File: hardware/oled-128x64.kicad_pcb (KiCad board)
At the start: 2 copper layers, 45 x 25 mm, 24 parts, among them P1 CON-SENSOR, U1 M24C64, U2 OLED013, U3 DRILL, U4 DRILL, U5 DRILL, U6 DRILL

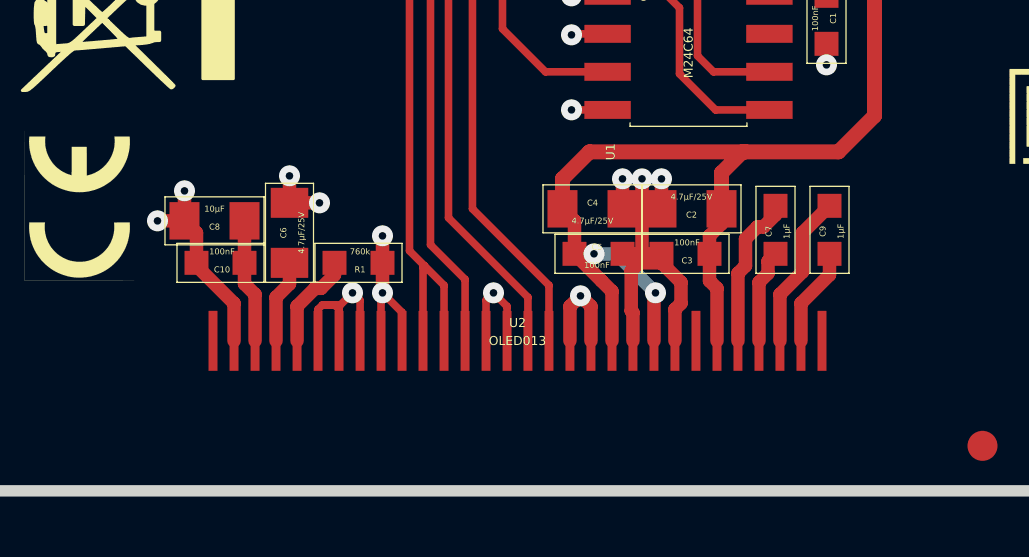
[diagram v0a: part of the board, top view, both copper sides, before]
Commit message: connect nc pins with gnd
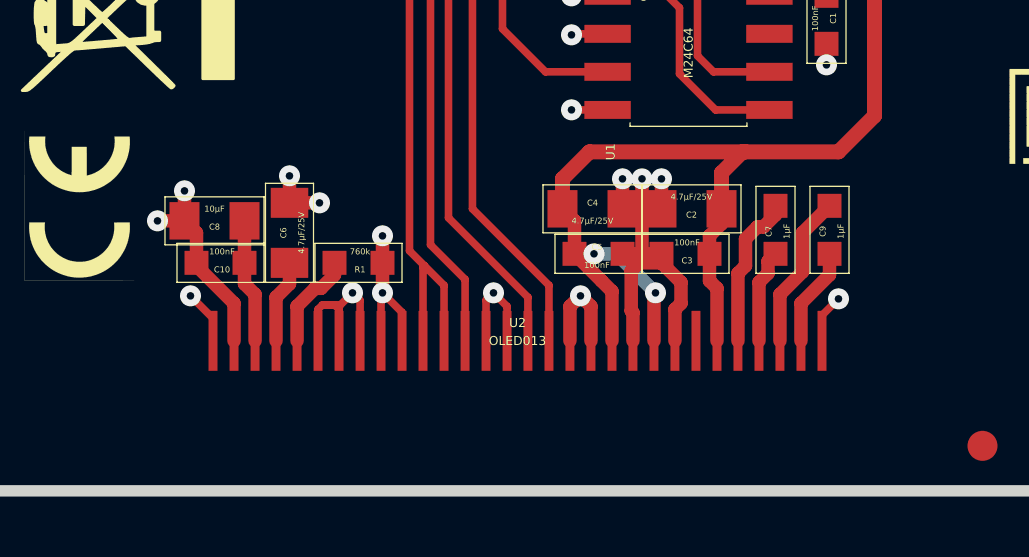
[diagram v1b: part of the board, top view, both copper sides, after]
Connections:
- U2 pad 1: (no net) -> GND
- U2 pad 30: (no net) -> GND
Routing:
- net GND: track 52.6 -> 56.0 mm, vias 21 -> 23

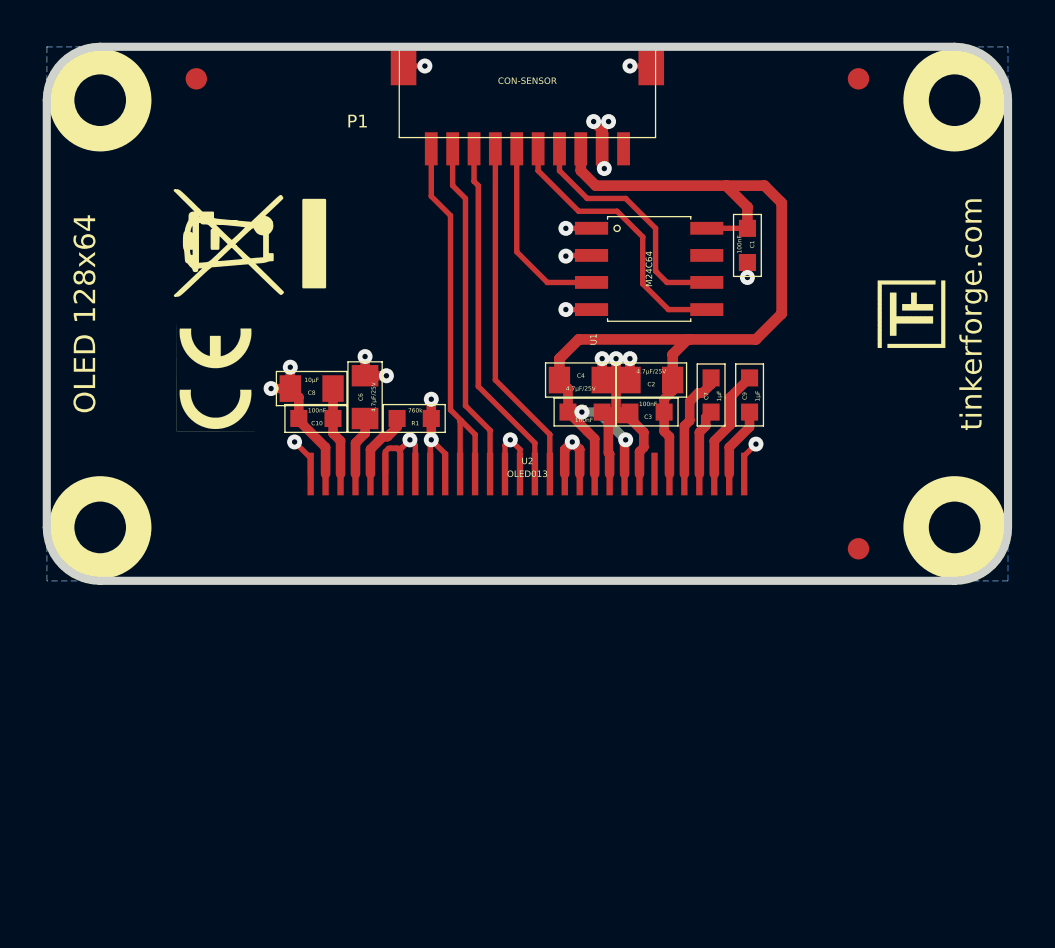
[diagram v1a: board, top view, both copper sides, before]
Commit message: change dimensions
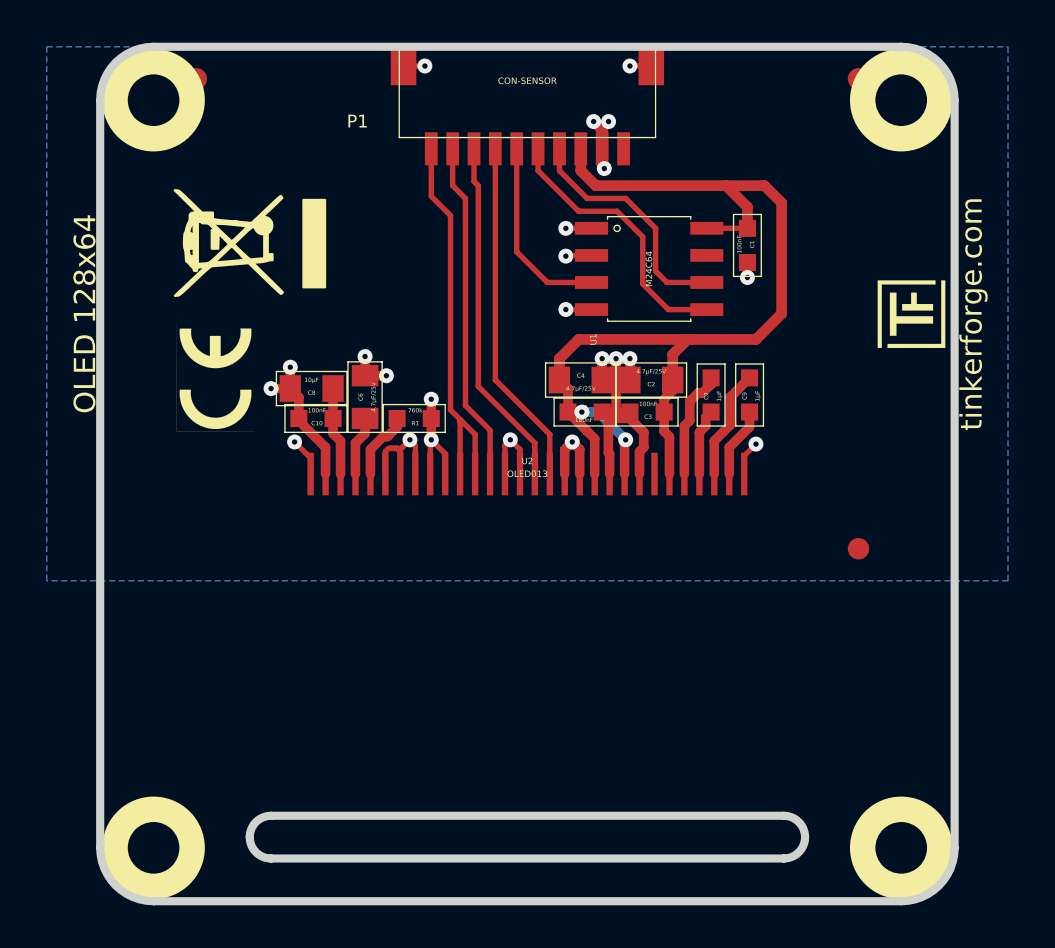
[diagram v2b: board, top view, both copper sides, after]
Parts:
- moved U3 15.2 mm to (136.6, 159.1)
- moved U6 15.2 mm to (171.6, 159.1)
- moved U4 2.50 mm to (136.6, 124.1)
- moved U5 2.50 mm to (171.6, 124.1)
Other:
- board size 45 x 25 mm -> 40 x 40 mm

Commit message: fix cutout position for lcd cable
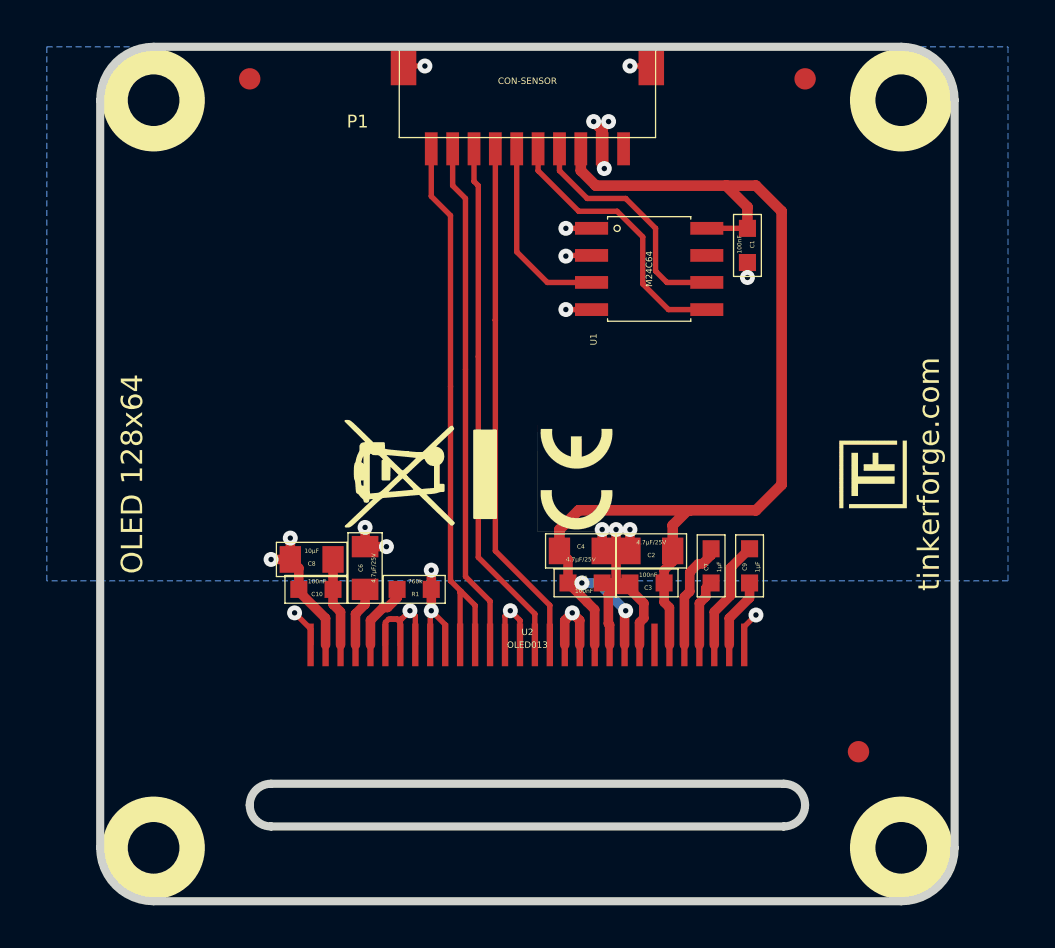
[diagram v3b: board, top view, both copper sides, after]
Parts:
- moved VAL 17.5 mm to (156.4, 141.8)
- moved G*** 13.4 mm to (149.1, 141.6)
- moved Fiducial_Mark 9.50 mm to (169.6, 154.6)
- moved C10 8.00 mm to (144.2, 147.0)
- moved C2 8.00 mm to (159.9, 145.2)
- moved C3 8.00 mm to (159.7, 146.7)
- moved C4 8.00 mm to (156.6, 145.2)
- moved C5 8.00 mm to (156.8, 146.7)
- moved C6 8.00 mm to (146.5, 146.0)
- moved C7 8.00 mm to (162.7, 145.9)
- moved C8 8.00 mm to (144.0, 145.6)
- moved C9 8.00 mm to (164.5, 145.9)
- moved R1 8.00 mm to (148.8, 147.0)
- moved U2 8.00 mm to (154.1, 149.6)
- moved G*** 7.71 mm to (168.7, 143.2)
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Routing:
- net Net-(P1-Pad7): track 16.3 -> 24.3 mm
- net Net-(P1-Pad9): track 16.0 -> 24.0 mm
- net Net-(P1-Pad8): track 16.4 -> 24.4 mm
- net Net-(P1-Pad10): track 18.6 -> 26.6 mm
- net 3V3: track 49.7 -> 57.5 mm
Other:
- outline, holes or cut-outs redrawn
